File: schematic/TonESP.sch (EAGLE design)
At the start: 13 parts, among them IC1 MCP23017SS

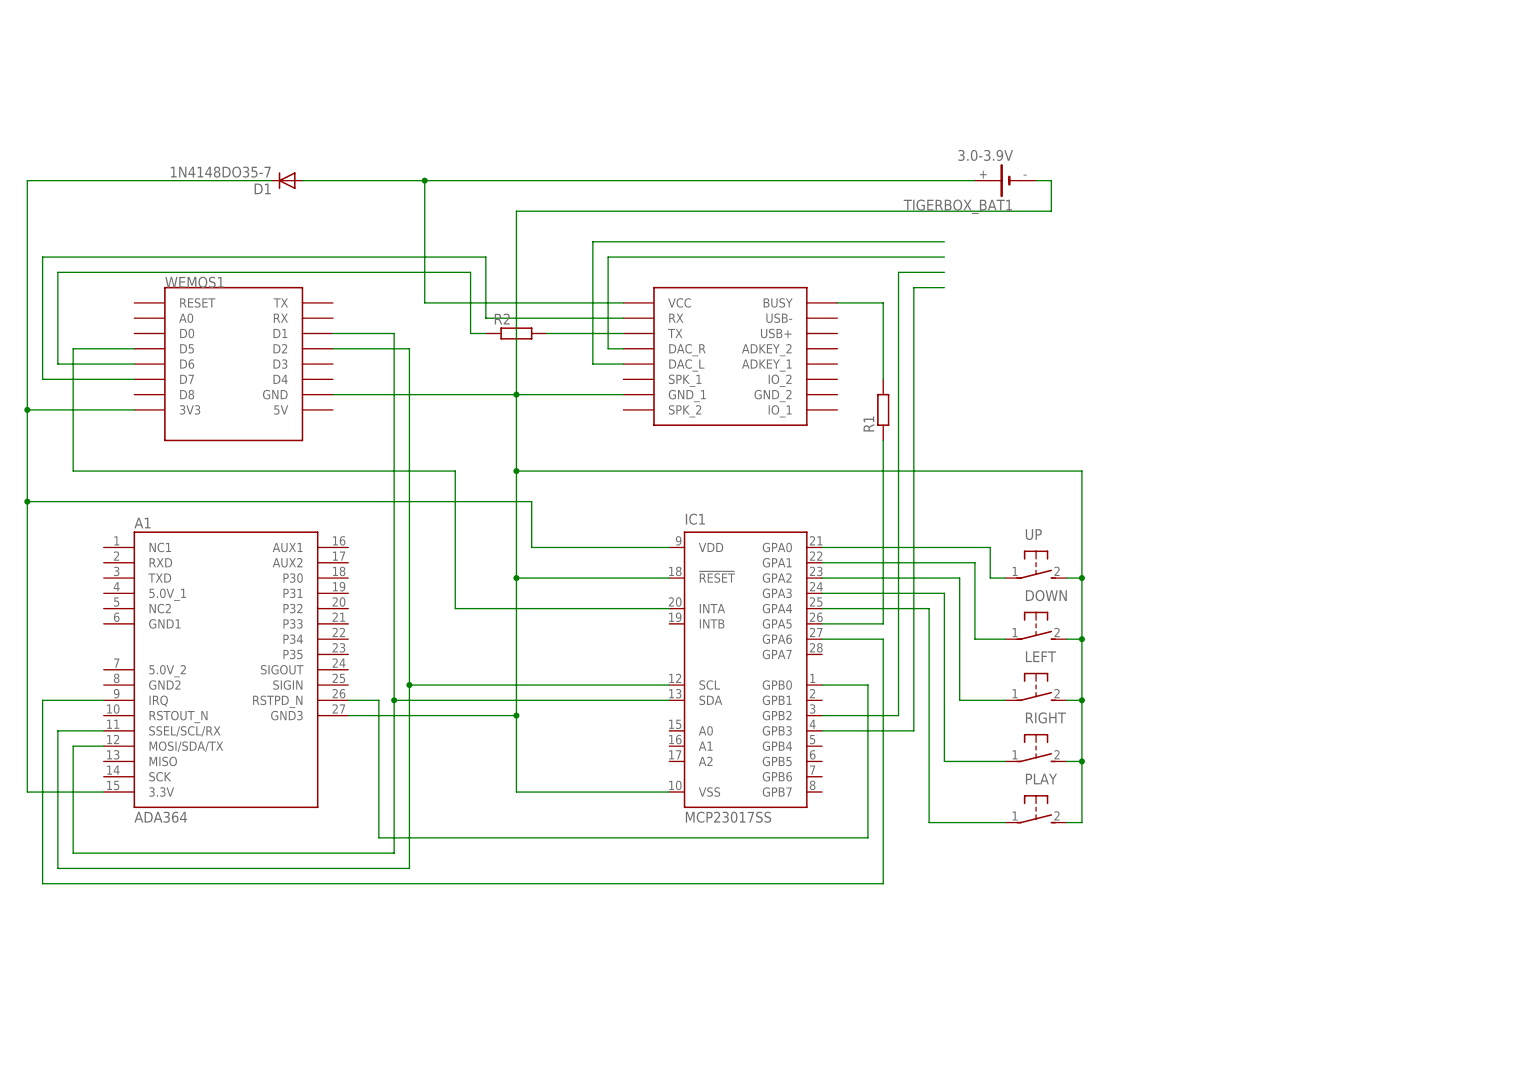
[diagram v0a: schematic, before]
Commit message: updated schematics, added backup text file
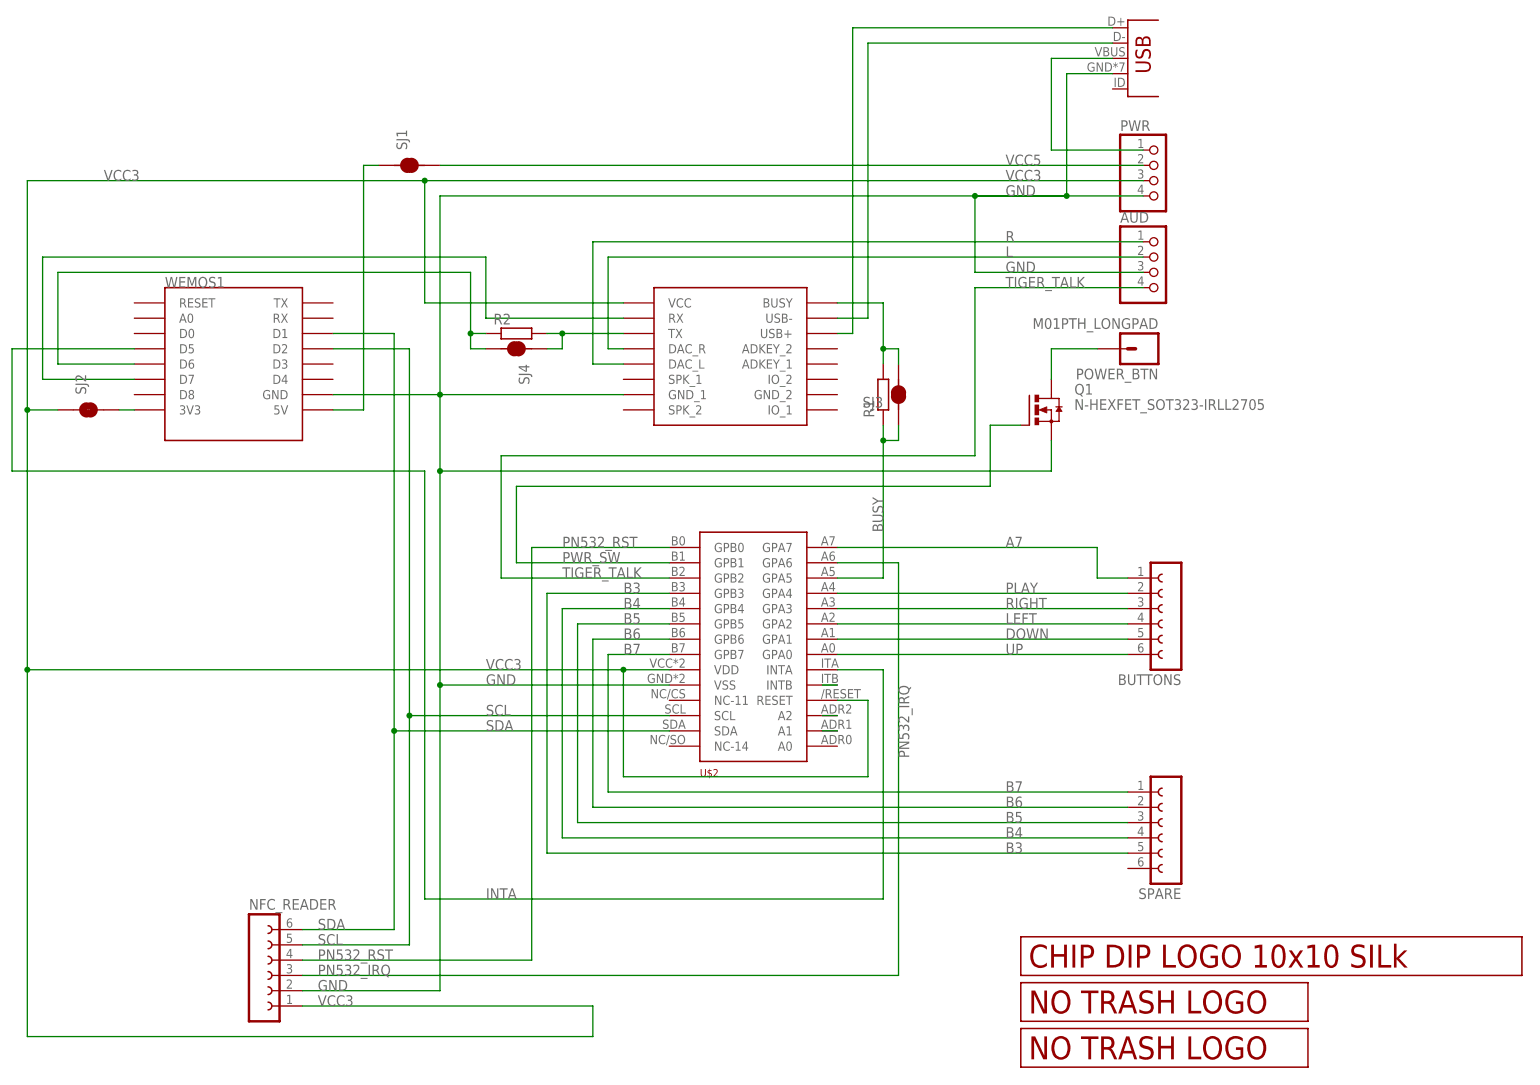
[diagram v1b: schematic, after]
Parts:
- removed A1: ADA364, ADA364:ADA364
- removed D1: 1N4148DO35-7, diode:1N4148DO35-7
- removed DOWN, LEFT, PLAY, RIGHT, UP: (no value), switch-omron:31-XX
- removed IC1: MCP23017SS, microchip:MCP23017SS
- removed TIGERBOX_BAT1: 3.0-3.9V, battery:CH291-1220LF
- added AUD, PWR: (no value), pinhead:PINHD-1X4
- added BUTTONS, NFC_READER, SPARE: (no value), con-lsta:FE06-1
- added JP1: USBUSB-MICROB-SMT-DIP, JKW_CHIP:USBUSB-MICROB-SMT-DIP
- added POWER_BTN: M01PTH_LONGPAD, SparkFun:M01PTH_LONGPAD
- added Q1: N-HEXFET_SOT323-IRLL2705, transistor-power:N-HEXFET_SOT323-IRLL2705
- added SJ1, SJ3, SJ4: (no value), JKW_CHIP:SMD_SJ_2WAY_CLOSEDCLOSED
- added SJ2: (no value), JKW_CHIP:SMD_SJ_2WAY_OPEN
- added U$2: (no value), IO-Expanders:MCP23017-E/SP
- added U$4: LOGO_10X10_SILK, JKW_CHIP:LOGO_10X10_SILK
- added U$5: LOGO_NO_TRASHNO_TRASH, JKW_CHIP:LOGO_NO_TRASHNO_TRASH
- added U$6: LOGO_NO_TRASHROHS, JKW_CHIP:LOGO_NO_TRASHROHS
- R1, R2: device rcl:R-EU_0204/7 -> resistor:R-EU_M0805
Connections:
- removed net N$10: A1.SSEL/SCL/RX, IC1.SCL, WEMOS1.D2
- removed net N$16: A1.IRQ, IC1.GPA6
- removed net N$17: A1.RSTPD_N, IC1.GPB0
- removed net N$18: A1.3.3V, D1.C, IC1.VDD, WEMOS1.3V3
- removed net N$19: U$1.DAC_L
- removed net N$2: A1.GND3, DOWN.S, IC1.!RESET, IC1.VSS, LEFT.S, PLAY.S, RIGHT.S, TIGERBOX_BAT1.-, U$1.GND_1, UP.S, WEMOS1.GND
- removed net N$20: D1.A, TIGERBOX_BAT1.+, U$1.VCC
- removed net N$21: IC1.GPB2
- removed net N$23: IC1.GPB3
- new net A7: BUTTONS.1, U$2.GPA7
- new net B3: SPARE.5, U$2.GPB3
- new net B4: SPARE.4, U$2.GPB4
- new net B5: SPARE.3, U$2.GPB5
- new net B6: SPARE.2, U$2.GPB6
- new net B7: SPARE.1, U$2.GPB7
- new net BUSY: R1.1, SJ3.1, U$2.GPA5
- new net DOWN: BUTTONS.5, U$2.GPA1
- new net GND: AUD.3, JP1.GND, NFC_READER.2, PWR.4, Q1.S, U$1.GND_1, U$2.VSS, WEMOS1.GND
- new net INTA: U$2.INTA, WEMOS1.D5
- new net L: AUD.2, U$1.DAC_R
- new net LEFT: BUTTONS.4, U$2.GPA2
- new net PLAY: BUTTONS.2, U$2.GPA4
- new net PN532_IRQ: NFC_READER.3, U$2.GPA6
- new net PN532_RST: NFC_READER.4, U$2.GPB0
- new net PWR_SW: Q1.G, U$2.GPB1
- new net R: AUD.1, U$1.DAC_L
- new net RIGHT: BUTTONS.3, U$2.GPA3
- new net SCL: NFC_READER.5, U$2.SCL, WEMOS1.D2
- new net SDA: NFC_READER.6, U$2.SDA, WEMOS1.D1
- new net TIGER_TALK: AUD.4, U$2.GPB2
- new net UP: BUTTONS.6, U$2.GPA0
- new net VCC3: NFC_READER.1, PWR.3, SJ2.1, U$1.VCC, U$2.RESET, U$2.VDD
- new net VCC5: PWR.2, SJ1.3
- net N$1: now also SJ2.3, WEMOS1.3V3; no longer U$1.DAC_R
- net N$11: now also JP1.D-, U$1.USB-; no longer IC1.GPA0, UP.P
- net N$12: now also JP1.D+, U$1.USB+; no longer DOWN.P, IC1.GPA1
- net N$13: now also U$2.INTB; no longer IC1.GPA2, LEFT.P
- net N$14: now also U$2.A2; no longer IC1.GPA3, RIGHT.P
- net N$15: now also U$2.A1; no longer IC1.GPA4, PLAY.P
- net N$3: now also SJ1.1, WEMOS1.5V; no longer IC1.GPA5, R1.1
- net N$4: now also SJ3.3
- net N$5: now also SJ4.1
- net N$6: now also SJ4.3
- net N$8: now also POWER_BTN.1, Q1.D; no longer IC1.INTA, WEMOS1.D5
- net N$9: now also JP1.VBUS, PWR.1; no longer A1.MOSI/SDA/TX, IC1.SDA, WEMOS1.D1
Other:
- moved on the sheet: R1
